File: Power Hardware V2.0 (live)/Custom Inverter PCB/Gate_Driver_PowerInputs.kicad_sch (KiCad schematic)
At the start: 29 parts, among them J1 1714971, J2 1714971, J3 1714968, J4 SSQ-110-03-G-D, J5 SSQ-110-03-G-D, K1 1-1393210-3, K2 1-1393210-3, Q7 HCPL-181-06BE, Q8 HCPL-181-06BE, U1 DRV8300DIPWR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

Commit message: switches instead of relays. Short on half bridge fixed. encoder page made. root page connections fixed
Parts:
- removed J4, J5: SSQ-110-03-G-D, SSQ_110_03_G_D (1):SAMTEC_SSQ-110-03-G-D, symbol SSQ-110-03-G-D:SSQ-110-03-G-D
- removed K1: 1-1393210-3, T9AS1D12_12:TE_1-1393210-3, symbol T9As1d12-12:1-1393210-3
- removed Q7, Q8: HCPL-181-06BE, HCPL_181_06BE:HCPL-181_BRA, symbol HCPL-181-06Be:HCPL-181-06BE
- removed R16, R17: 330, Resistor_SMD:R_0805_2012Metric, symbol Device:R
- removed U2, U3: NTR4170NT1G, NTR4170NT1G:SOT-23_ONS, symbol 2025-02-22_21-00-42:NTR4170NT1G
- added S1, S2: 100SP1T1B4M2QE, 100SP1T1B4M2QE:SW_100SP1T1B4M2QE, symbol 100SP1T1B4M2QE:100SP1T1B4M2QE
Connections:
- net GND: now also K2.A2
- net +12V renamed +12VDC
- net +12VDC: now also S1.1, S2.2
- net +12V - to relay: no longer names the net of K2.A1
- net +12V - to relay: now also S2.1; no longer J1.2
- net +3.3V renamed +3.3VDC
- new net +12V to relay: J1.2, S1.2
- no-connect marks 0 -> 2
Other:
- note added: "INTERFACE INPUTS"
- note added: "INTERFACE OUTPUTS"
- note removed: "INTERFACE"
- note removed: "MCU INPUTS"
- moved on the sheet: C1, C2, VR1

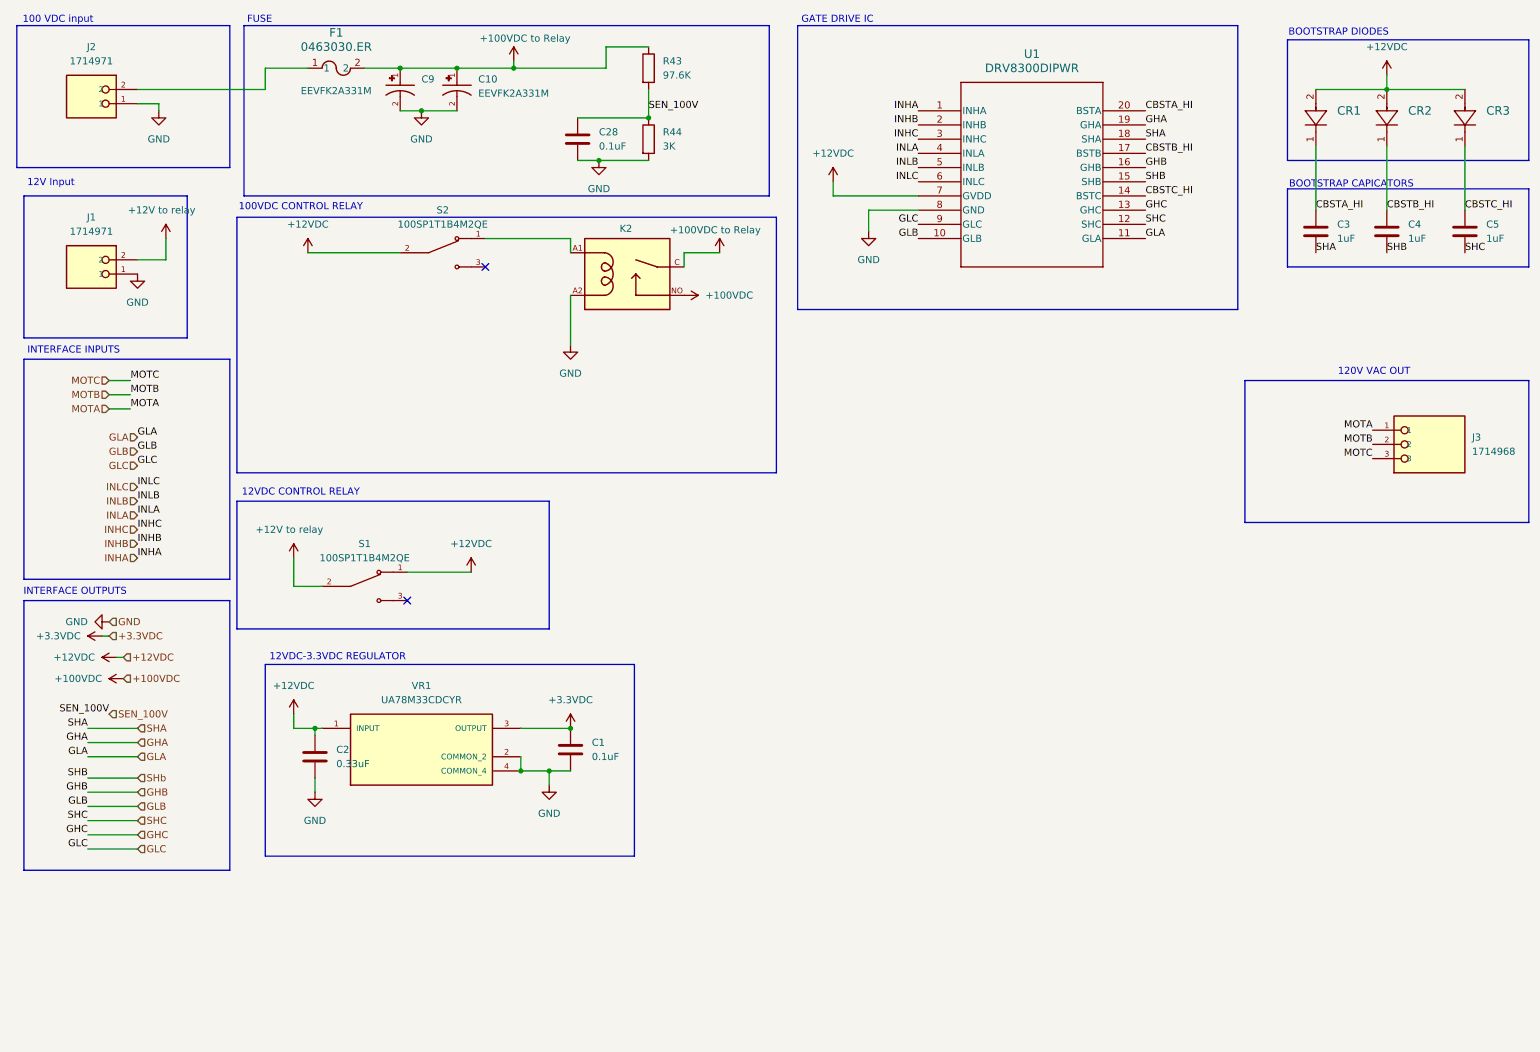
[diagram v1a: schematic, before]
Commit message: Schematic Changes
-Changed 3.3V regulator to a higher power unit for the sin-cos circuit (from 500mA to 3A)
-Fixed flipped MOTA,B,C connection to Output Terminal
- Current Sense IC setup
- Fuses for Phase current outputs
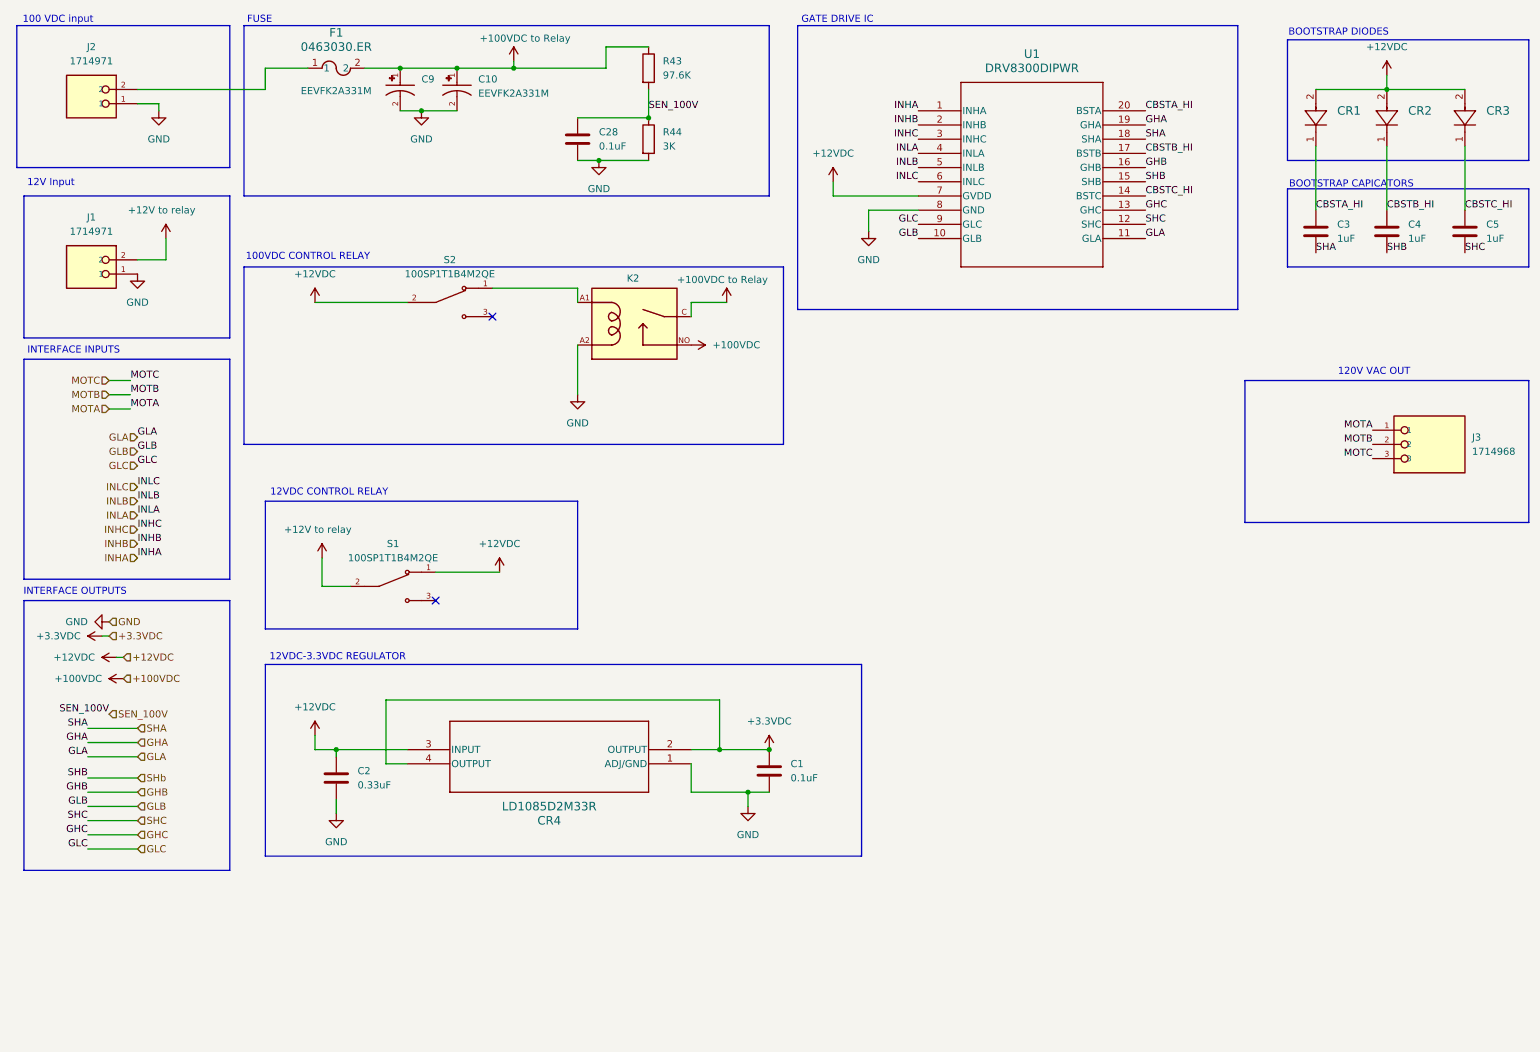
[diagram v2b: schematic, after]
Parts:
- removed VR1: UA78M33CDCYR, UA78M33CDCYR:VREG_UA78M33CDCYR, symbol UA78M33CDCYR:UA78M33CDCYR
- added CR4: LD1085D2M33R, D2PAK/A_STM, symbol 3.3V Regulator:LD1085D2M33R
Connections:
- net +12VDC: now also CR4.3 (INPUT)
- net +3.3VDC: now also CR4.2 (OUTPUT), CR4.4 (OUTPUT)
- net GND: now also CR4.1 (ADJ/GND)
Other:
- moved on the sheet: C1, C2, K2, S1, S2

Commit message: no changes
no
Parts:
- removed S1, S2: 100SP1T1B4M2QE, 100SP1T1B4M2QE:SW_100SP1T1B4M2QE, symbol 100SP1T1B4M2QE:100SP1T1B4M2QE
- added J7, J8: 1714971, 1714971:PHOENIX_1714971, symbol 1714971:1714971
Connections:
- net +12V to relay: now also J8.2
- net +12VDC: now also J7.2, J8.1
- net at K2.A1: now also J7.1
- no-connect marks 2 -> 0
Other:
- note added: "Screw terminals to external switches"

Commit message: no major changes
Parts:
- F1: footprint 0463030.ER:FUSE_0463_LTF -> 0463030ERFUSE:FUSE_0463_LTF-L
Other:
- note added: "100VDC CONTROL RELAY + SWITCH"
- note added: "12VDC CONTROL SWITCH"
- note removed: "100VDC CONTROL RELAY"
- note removed: "12VDC CONTROL RELAY"
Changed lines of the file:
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@@
 		)
 	)
-	(text "100VDC CONTROL RELAY\n"
-		(exclude_from_sim no)
-		(at 64.77 56.642 0)
+	(text "100VDC CONTROL RELAY + SWITCH\n"
+		(exclude_from_sim no)
+		(at 69.596 56.642 0)
 		(effects
 			(font
@@
 		)
 	)
-	(text "12VDC CONTROL RELAY\n"
+	(text "12VDC CONTROL SWITCH\n\n"
 		(exclude_from_sim no)
 		(at 68.58 98.806 0)
@@
 			)
 		)
-		(property "Footprint" "0463030.ER:FUSE_0463_LTF"
+		(property "Footprint" "0463030ERFUSE:FUSE_0463_LTF-L"
 			(at 64.77 22.86 0)
 			(effects

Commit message: Sine-cos test
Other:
- note added: "Motor Output"
- note removed: "120V VAC OUT"
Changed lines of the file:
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@@
 		)
 	)
-	(text "120V VAC OUT"
+	(text "Motor Output\n"
 		(exclude_from_sim no)
 		(at 255.524 77.216 0)

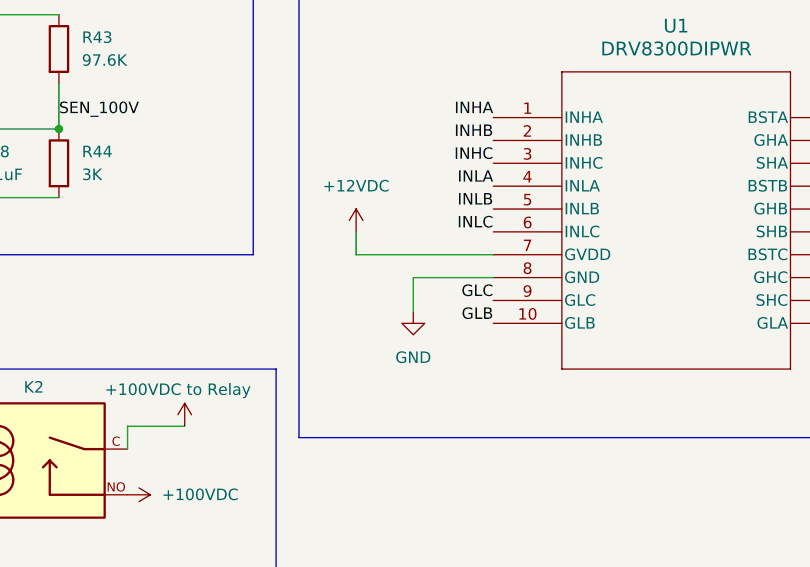
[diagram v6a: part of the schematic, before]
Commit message: Resolver Reading opamps
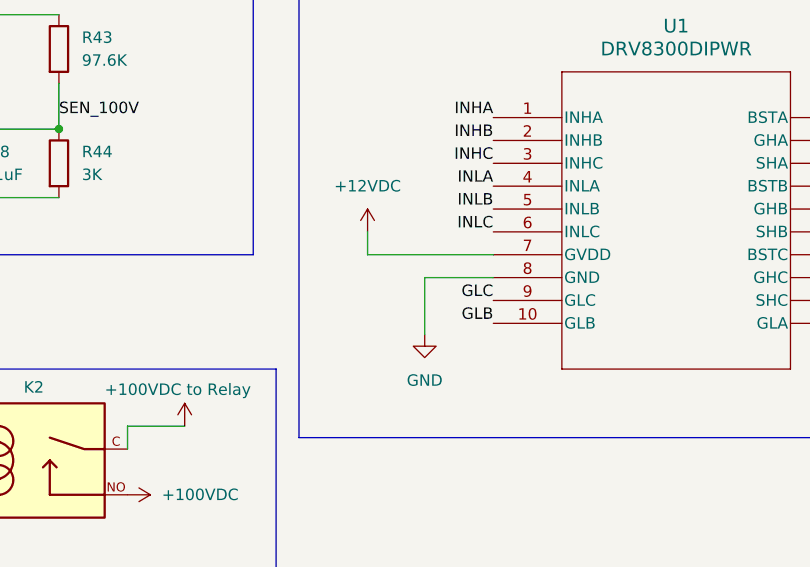
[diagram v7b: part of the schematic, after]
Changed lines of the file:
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@@
 	(generator_version "9.0")
 	(paper "A4")
+	(title_block
+		(date "2025-04-19")
+		(rev "1")
+	)
 	(rectangle
 		(start 240.03 44.45)
@@
 	(wire
 		(pts
-			(xy 158.75 45.72) (xy 158.75 43.18)
+			(xy 160.02 45.72) (xy 160.02 43.18)
 		)
 		(stroke
@@
 	(wire
 		(pts
-			(xy 173.99 48.26) (xy 165.1 48.26)
+			(xy 173.99 48.26) (xy 166.37 48.26)
 		)
 		(stroke
@@
 	(wire
 		(pts
-			(xy 173.99 45.72) (xy 158.75 45.72)
+			(xy 173.99 45.72) (xy 160.02 45.72)
 		)
 		(stroke
@@
 	(wire
 		(pts
-			(xy 165.1 48.26) (xy 165.1 52.07)
+			(xy 166.37 48.26) (xy 166.37 54.61)
 		)
 		(stroke
@@
 	(symbol
 		(lib_id "power:GND")
-		(at 165.1 52.07 0)
+		(at 166.37 54.61 0)
 		(unit 1)
 		(exclude_from_sim no)
@@
 		(fields_autoplaced yes)
 		(property "Reference" "#PWR08"
-			(at 165.1 58.42 0)
+			(at 166.37 60.96 0)
 			(effects
 				(font
@@
 		)
 		(property "Value" "GND"
-			(at 165.1 57.15 0)
+			(at 166.37 59.69 0)
 			(effects
 				(font
@@
 		)
 		(property "Footprint" ""
-			(at 165.1 52.07 0)
+			(at 166.37 54.61 0)
 			(effects
 				(font
@@
 		)
 		(property "Datasheet" ""
-			(at 165.1 52.07 0)
+			(at 166.37 54.61 0)
 			(effects
 				(font
@@
 		)
 		(property "Description" "Power symbol creates a global label with name \"GND\" , ground"
-			(at 165.1 52.07 0)
+			(at 166.37 54.61 0)
 			(effects
 				(font
@@
 	(symbol
 		(lib_id "power:+12V")
-		(at 158.75 43.18 0)
+		(at 160.02 43.18 0)
 		(unit 1)
 		(exclude_from_sim no)
@@
 		(fields_autoplaced yes)
 		(property "Reference" "#PWR06"
-			(at 158.75 46.99 0)
+			(at 160.02 46.99 0)
 			(effects
 				(font
@@
 		)
 		(property "Value" "+12VDC"
-			(at 158.75 38.1 0)
+			(at 160.02 38.1 0)
 			(effects
 				(font
@@
 		)
 		(property "Footprint" ""
-			(at 158.75 43.18 0)
+			(at 160.02 43.18 0)
 			(effects
 				(font
@@
 		)
 		(property "Datasheet" ""
-			(at 158.75 43.18 0)
+			(at 160.02 43.18 0)
 			(effects
 				(font
@@
 		)
 		(property "Description" "Power symbol creates a global label with name \"+12V\""
-			(at 158.75 43.18 0)
+			(at 160.02 43.18 0)
 			(effects
 				(font

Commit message: footprint lib fixes
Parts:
- CR4: footprint D2PAK/A_STM -> LD1085D2M33R:D2PAK&slash_A_STM
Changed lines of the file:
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@@
 			)
 		)
-		(property "Footprint" "D2PAK/A_STM"
+		(property "Footprint" "LD1085D2M33R:D2PAK&slash_A_STM"
 			(at 133.35 147.32 0)
 			(effects
